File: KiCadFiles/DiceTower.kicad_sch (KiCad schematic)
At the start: 27 parts, among them J1 USB_C_Receptacle_PowerOnly_6P, J2 Conn_01x05_Socket, J3 Conn_01x02_Pin, SW0 ChMxBl, SW1 ChMxBl, SW2 ChMxBl, SW3 ChMxBl, SW4 ChMxBl, SW5 ChMxBl, SW6 ChMxBl, U1 NHD-0420H1Z, U3 TPS73131DBV

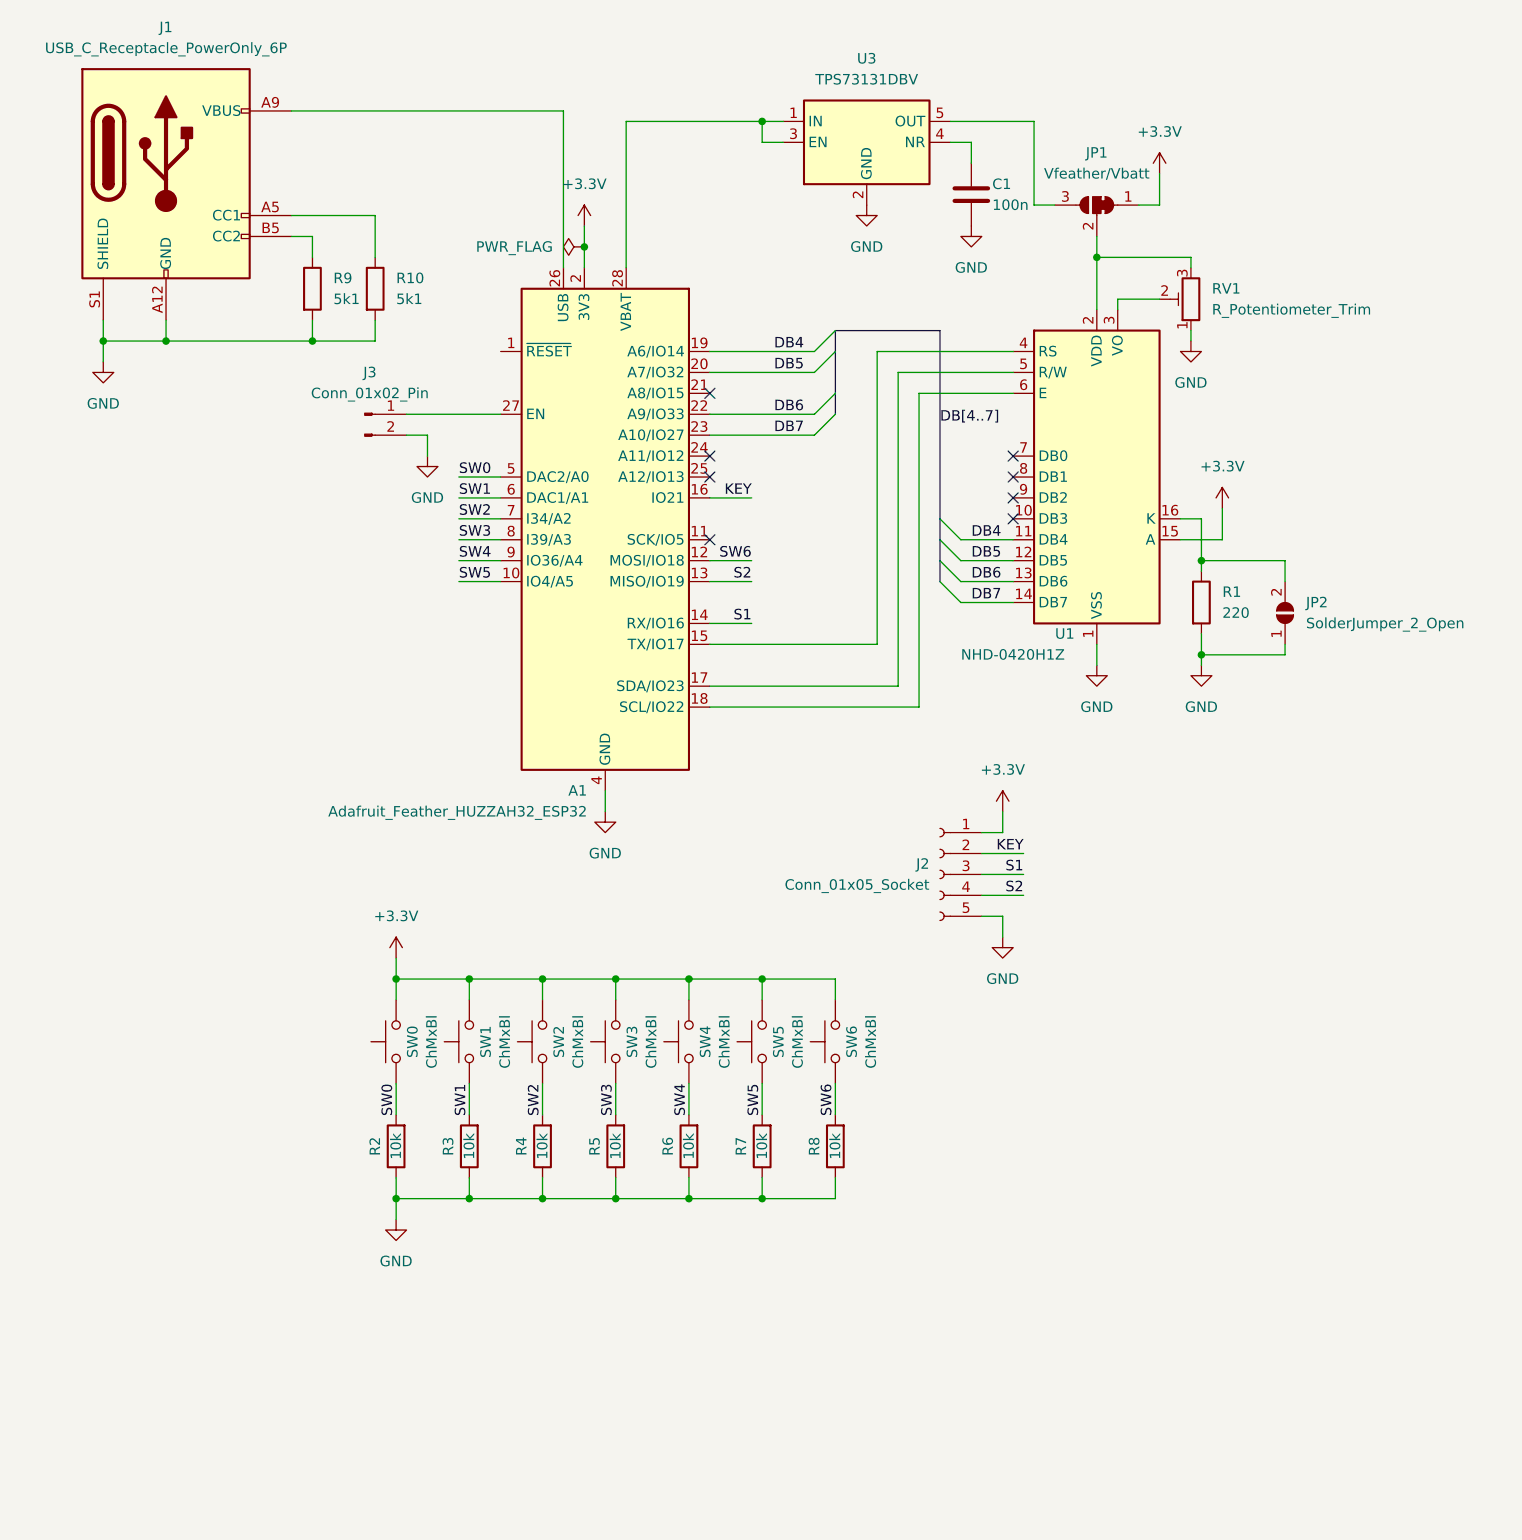
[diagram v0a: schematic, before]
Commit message: Add mounting holes
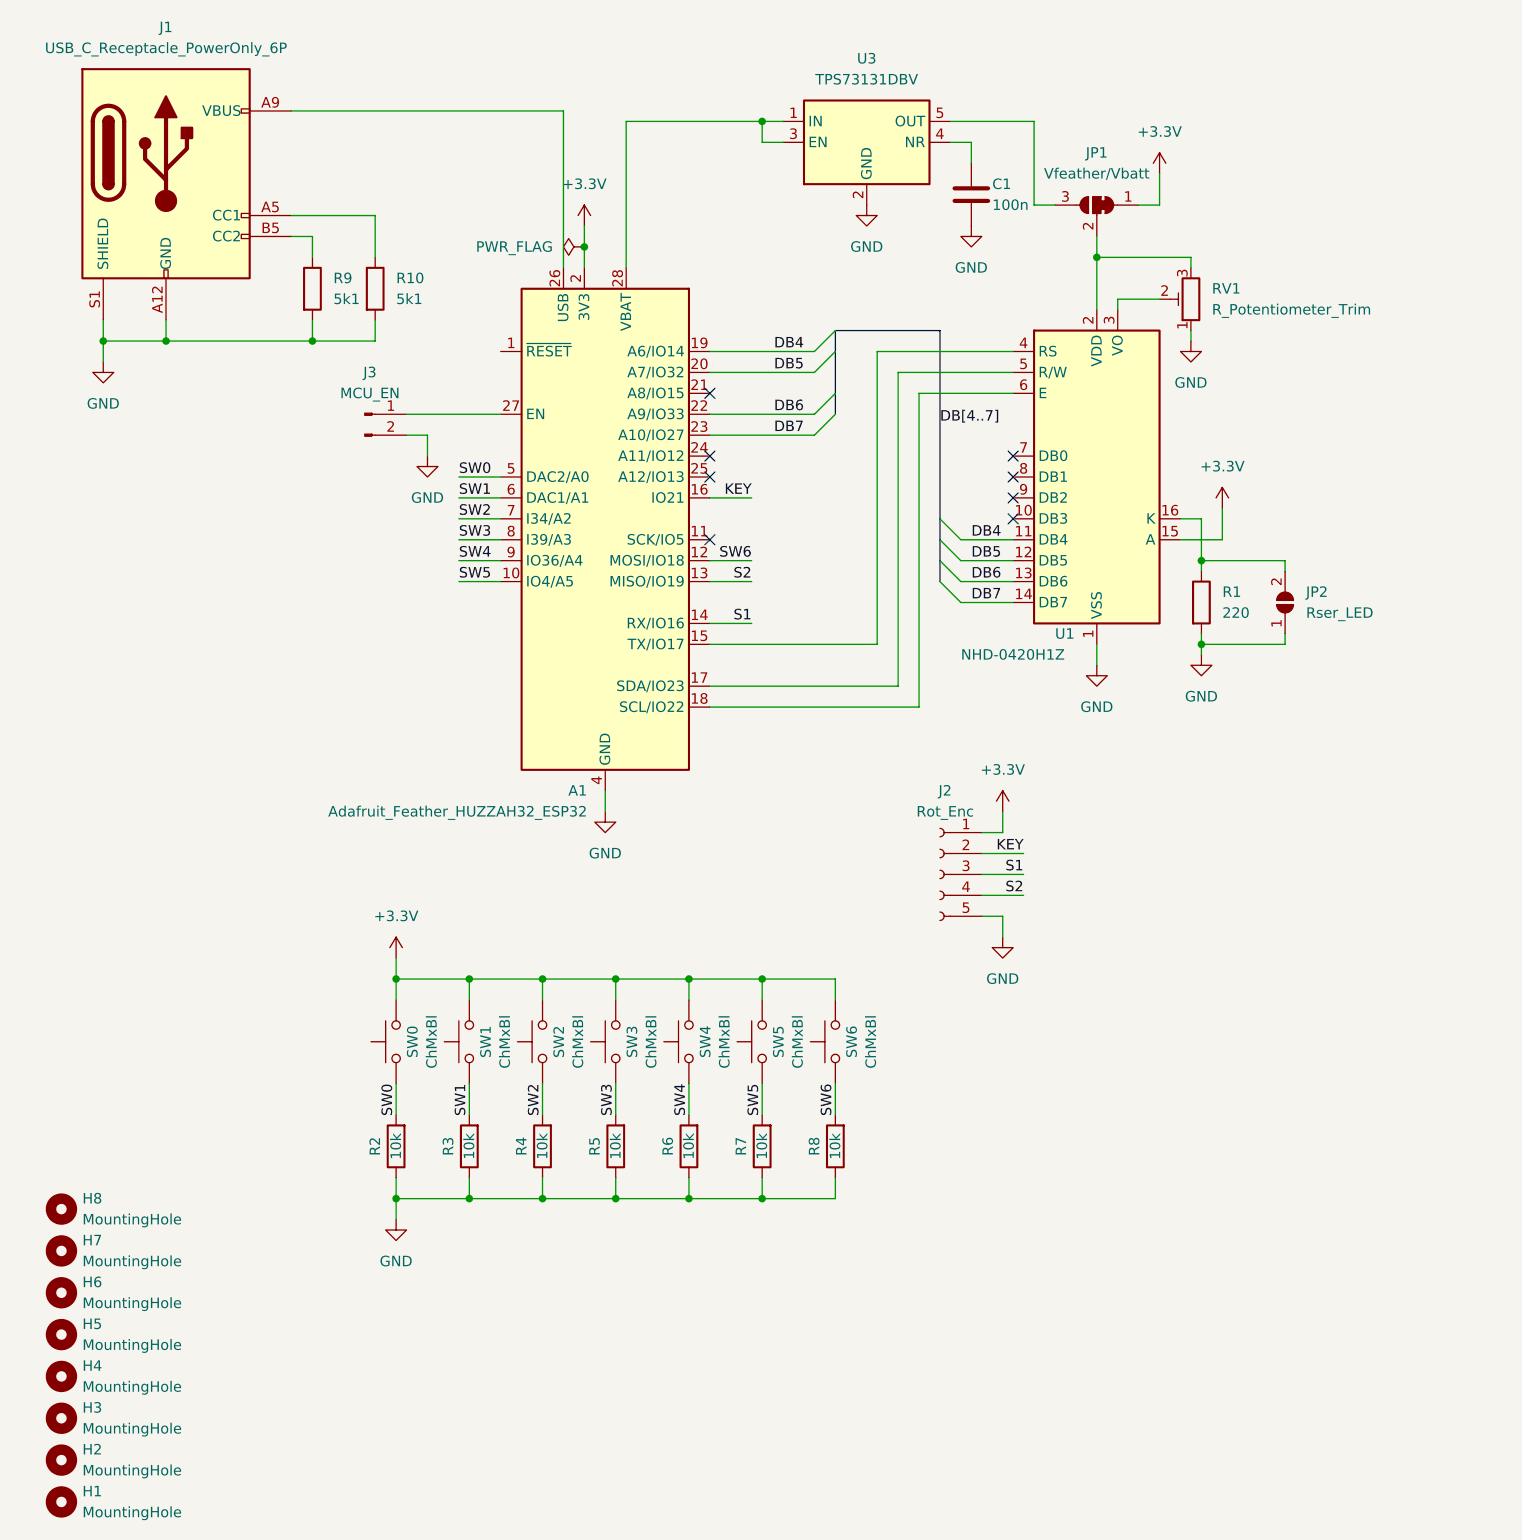
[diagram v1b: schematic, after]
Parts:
- added H1, H2, H3, H4, H5, H6, H7, H8: MountingHole, MountingHole:MountingHole_3.2mm_M3_ISO14580, symbol Mechanical:MountingHole
- J2: value Conn_01x05_Socket -> Rot_Enc
- J3: value Conn_01x02_Pin -> MCU_EN
- JP2: value SolderJumper_2_Open -> Rser_LED
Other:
- moved on the sheet: JP2
